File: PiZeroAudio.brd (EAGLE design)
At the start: 160 x 100 mm, 10 parts, among them J1 1X2-3.5MM

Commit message: Added I2C and Amplifier
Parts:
- added C10, C15, C16, C20, C22, C25: 1nF, resistor:C0805
- added C11, C26, C5, C6, C8, C9: 100nF, adafruit:C0805
- added C12: 100uF, adafruit:C0805
- added C13, C17, C18, C23: 220nF, resistor:C0805
- added C14, C19, C21, C24: 1uF, resistor:C0805
- added C27: 100UF, adafruit:C0805
- added C7: 47uF, adafruit:085CS_1AR
- added CN1: 1X4-BIG, adafruit:1X04-BIG
- added L1, L2, L3, L4: BLM31A, HappyBrackets:SML1206
- added R10: 39K, adafruit:R0805
- added R11: 56K, adafruit:R0805
- added R12, R13, R14: 33K, adafruit:R0805
- added R15: 10R, adafruit:R0805
- added R5, R8: 1K8, adafruit:R0805
- added R6: 220, adafruit:R0805
- added R7: 100, adafruit:R0805
- added R9: 10K, adafruit:R0805
- added U1: (no value), adafruit:TSSOP14
- added U2: (no value), HappyBrackets:LGA-16-3X3
- added U3: NC7WZ16, fairchild:SC-70-6
- added U4: TPA3144D2PWPR, HappyBrackets:HTSSOP28
- C1, C2: value 33nF -> 100nF
- C4: value 47uF -> 100nF; device adafruit:085CS_1AR -> adafruit:C0805
- R1: value 270 -> 10K
- R2: value 150 -> 10K
- R3: value 270 -> 220
- R4: value 150 -> 100
- moved R2 118.0 mm to (-82.5, -53.3)
- moved C2 98.0 mm to (-82.5, -59.7)
- moved R1 84.4 mm to (-82.5, -47.0)
- moved C1 82.4 mm to (-82.5, -40.6)
- moved R3 39.4 mm to (-59.7, 34.3)
- moved C4 10.5 mm to (-48.3, 34.3)
- moved R4 10.2 mm to (-16.5, 44.5)
- renumbered U$1 to CON1
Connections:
- new net +3V3: C1.1, C5.1, C6.1, C8.1, CON1.1, R1.1, R2.1, U1.1, U2.1, U2.16, U2.4, U2.5, U3.5
- new net /MUTE: R9.1
- new net AUDIO-L: C3.-, R5.2
- new net AUDIO-R: C7.-, R8.2, U4.12
- new net N$10: C23.2, U4.17
- new net N$11: C16.2, CN1.2, L2.C
- new net N$12: C15.1, CN1.1, L1.C
- new net N$13: C18.2, U4.21
- new net N$14: C20.1, CN1.3, L3.C
- new net N$15: C22.2, CN1.4, L4.C
- new net N$16: C17.2, U4.22
- new net N$17: C13.2, U4.26
- new net N$18: C13.1, L1.A, U4.25
- new net N$19: C17.1, L2.A, U4.23
- new net N$2: R3.2, U3.6
- new net N$20: C18.1, L3.A, U4.20
- new net N$21: C23.1, L4.A, U4.18
- new net N$23: R12.1, R13.2, U4.6
- new net N$24: R13.1, R14.2, U4.7
- new net N$25: R10.1, R11.2, U4.8
- new net N$26: C19.1, R11.1, R14.1, U4.5, U4.9
- new net N$4: C7.+, C9.1, R6.1, R7.2
- new net N$5: R9.2, U4.1, U4.2
- new net N$6: U4.3
- new net N$7: C14.1, U4.4
- new net N$8: C21.1, U4.11
- new net N$9: C24.1, R15.1, U4.14
- new net SCL: CON1.5, R2.2, U2.2
- new net SDA: CON1.3, R1.2, U2.3
- net +5V: now also C10.1, C11.1, C12.1, C2.1, C25.1, C26.1, C27.1, R15.2, U1.14, U4.15, U4.16, U4.27, U4.28
- net GND: now also C10.2, C11.2, C12.2, C14.2, C15.2, C16.1, C19.2, C20.2, C21.2, C22.1, C24.2, C25.2, C26.2, C27.2, C4.2, C5.2, C6.2, C8.2, C9.2, R10.2, R12.2, R5.1, R7.1, R8.1, U1.7, U2.10, U2.11, U2.12, U2.13, U2.15, U2.8, U2.9, U3.2, U4.10, U4.13, U4.19, U4.24; no longer R2.1
- net N$1: now also C4.1, R3.1, R4.2; no longer C1.1, R1.1, R2.2
- net N$3: now also R6.2, U3.4; no longer C2.1, C4.+, R3.1, R4.2
- net PWM-LEFT: now also U3.1; no longer R1.2
- net PWM-RIGHT: now also U3.3; no longer R3.2
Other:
- board size 160 x 100 mm -> 65.4 x 30.2 mm

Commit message: Renumbered Pins Placed components for first board
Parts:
- removed C27: 100UF, adafruit:C0805
- added JP1: GPIO, adafruit:2X04
- C10, C25: value 1nF -> 100nF; device resistor:C0805 -> adafruit:C0805
- C11: value 100nF -> 100uF; device adafruit:C0805 -> adafruit:CT3528
- C12: value 100uF -> 220nF; device adafruit:C0805 -> resistor:C0805
- C13, C18, C23: value 220nF -> 1uF
- C14, C19, C21, C24: value 1uF -> 1nF
- C16, C22: value 1nF -> 220nF
- C20: value 1nF -> 1uF
- C26: value 100nF -> 100UF; device adafruit:C0805 -> adafruit:CT3528
- C3: device adafruit:085CS_1AR -> adafruit:CT3528
- C6: value 100nF -> 47uF; device adafruit:C0805 -> adafruit:CT3528
- C7: value 47uF -> 100nF; device adafruit:085CS_1AR -> adafruit:C0805
- C9: value 100nF -> 1nF; device adafruit:C0805 -> resistor:C0805
- L1, L2, L3, L4: value BLM31A -> FB
- moved R14 287.2 mm to (-33.1, 3.30)
- moved R13 283.1 mm to (-33.1, 5.46), turned to 180 degrees
- moved R12 279.0 mm to (-33.1, 7.62)
- moved R11 269.9 mm to (-39.2, 6.10)
- moved R10 261.2 mm to (-39.1, 3.43), turned to 180 degrees
- moved C23 259.4 mm to (-46.0, 15.9)
- moved C19 253.7 mm to (-67.3, 7.49), turned to 90 degrees
- moved C18 249.0 mm to (-46.0, 11.6)
- moved C17 240.7 mm to (-58.5, 12.1)
- moved C13 234.1 mm to (-45.8, 8.89)
- moved C22 230.4 mm to (-58.5, 14.2)
- moved C20 226.4 mm to (-46.0, 13.7)
- moved C16 213.6 mm to (-58.5, 9.78)
- moved C15 203.8 mm to (-65.2, 7.49), turned to 270 degrees
- moved L4 202.4 mm to (-69.7, 13.2), turned to 90 degrees
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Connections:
- new net ACC-INT1: CON1.11, U2.6
- new net ACC-INT2: CON1.13, U2.7
- new net GPIO21: CON1.29, U1.2
- new net GPIO22: CON1.31, U1.3
- new net GPIO23: CON1.33, U1.4
- new net GPIO25: CON1.37, U1.5
- new net L+: C14.1, CN1.1, L1.C
- new net L-: C15.2, CN1.2, L2.C
- new net R+: C21.2, CN1.4, L4.C
- new net R-: C19.1, CN1.3, L3.C
- net +3V3: now also C7.1, CON1.17, U1.8; no longer C6.1, C8.1
- net +5V: now also C11.+, C24.1, C26.+, C9.1; no longer C11.1, C12.1, C26.1, C27.1
- net /MUTE: now also CON1.36
- net AUDIO-L: now also C6.-, R8.2; no longer C3.-, R5.2
- net AUDIO-R: now also C3.-, R5.2; no longer C7.-, R8.2
- net GND: now also C11.-, C13.2, C15.1, C18.2, C21.1, C23.2, C26.-, C7.2, JP1.2, JP1.4, JP1.6, JP1.8; no longer C11.2, C12.2, C15.2, C16.1, C21.2, C22.1, C26.2, C27.2, C6.2
- net N$10: now also C22.2; no longer C23.2
- net N$11: now also JP1.1, U1.13; no longer C16.2, CN1.2, L2.C
- net N$12: now also JP1.3, U1.12; no longer C15.1, CN1.1, L1.C
- net N$13: now also C17.2; no longer C18.2
- net N$14: now also JP1.5, U1.11; no longer C20.1, CN1.3, L3.C
- net N$15: now also JP1.7, U1.10; no longer C22.2, CN1.4, L4.C
- net N$16: now also C16.2; no longer C17.2
- net N$17: now also C12.2; no longer C13.2
- net N$18: now also C12.1; no longer C13.1
- net N$19: now also C16.1; no longer C17.1
- net N$20: now also C17.1; no longer C18.1
- net N$21: now also C22.1; no longer C23.1
- net N$26: now also C18.1; no longer C19.1
- net N$4: now also C6.+, C8.1; no longer C7.+, C9.1
- net N$7: now also C13.1; no longer C14.1
- net N$8: now also C20.1; no longer C21.1
- net N$9: now also C23.1; no longer C24.1
- net PWM-LEFT: now also U3.3; no longer U3.1
- net PWM-RIGHT: now also CON1.35, U3.1; no longer CON1.33, U3.3

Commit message: Updated
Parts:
- moved JP1 0.90 mm to (-16.6, 18.2)
- moved U2 0.42 mm to (-69.1, 20.1), turned to 270 degrees
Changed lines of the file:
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@@
 <element name="R5" library="adafruit" package="R0805" value="1K8" x="-33.655" y="10.922" rot="R270"/>
 <element name="R8" library="adafruit" package="R0805" value="1K8" x="-39.243" y="13.716"/>
-<element name="U2" library="HappyBrackets" library_urn="urn:adsk.eagle:library:5224691" package="LGA-16-3X3" package3d_urn="urn:adsk.eagle:package:5224694/1" value="" x="-68.7956" y="20.32" rot="R90"/>
+<element name="U2" library="HappyBrackets" library_urn="urn:adsk.eagle:library:5224691" package="LGA-16-3X3" package3d_urn="urn:adsk.eagle:package:5224694/1" value="" x="-69.1264" y="20.066" rot="R270"/>
 <element name="C5" library="adafruit" package="C0805" value="100nF" x="-68.8292" y="23.622"/>
 <element name="C1" library="adafruit" package="C0805" value="100nF" x="-49.53" y="23.241"/>
@@
 <element name="R13" library="adafruit" package="R0805" value="33K" x="-33.147" y="5.461" rot="R180"/>
 <element name="R14" library="adafruit" package="R0805" value="33K" x="-33.147" y="3.302"/>
-<element name="JP1" library="adafruit" package="2X04" value="GPIO" x="-16.51" y="19.05" rot="R270"/>
+<element name="JP1" library="adafruit" package="2X04" value="GPIO" x="-16.637" y="18.161" rot="R270"/>
 </elements>
 <signals>
@@
 <wire x1="-60.21" y1="26.5" x2="-55.13" y2="29.04" width="0" layer="19" extent="1-1"/>
 <wire x1="-65.29" y1="29.04" x2="-60.21" y2="26.5" width="0" layer="19" extent="1-1"/>
-<wire x1="-69.7956" y1="21.72" x2="-65.29" y2="29.04" width="0" layer="19" extent="1-1"/>
-<wire x1="-69.2956" y1="21.72" x2="-69.7956" y2="21.72" width="0" layer="19" extent="1-1"/>
-<wire x1="-68.7956" y1="21.72" x2="-69.2956" y2="21.72" width="0" layer="19" extent="1-1"/>
-<wire x1="-68.2956" y1="21.72" x2="-68.7956" y2="21.72" width="0" layer="19" extent="1-1"/>
-<wire x1="-67.7956" y1="21.72" x2="-68.2956" y2="21.72" width="0" layer="19" extent="1-1"/>
-<wire x1="-69.2956" y1="21.72" x2="-67.7956" y2="21.72" width="0" layer="19" extent="1-1"/>
-<wire x1="-70.1956" y1="20.32" x2="-69.7956" y2="21.72" width="0" layer="19" extent="1-1"/>
-<wire x1="-67.9792" y1="23.622" x2="-69.2956" y2="21.72" width="0" layer="19" extent="1-1"/>
-<wire x1="-73.152" y1="21.756" x2="-70.1956" y2="20.32" width="0" layer="19" extent="1-1"/>
+<wire x1="-68.1264" y1="18.666" x2="-65.29" y2="29.04" width="0" layer="19" extent="1-1"/>
+<wire x1="-68.6264" y1="18.666" x2="-68.1264" y2="18.666" width="0" layer="19" extent="1-1"/>
+<wire x1="-69.1264" y1="18.666" x2="-68.6264" y2="18.666" width="0" layer="19" extent="1-1"/>
+<wire x1="-69.6264" y1="18.666" x2="-69.1264" y2="18.666" width="0" layer="19" extent="1-1"/>
+<wire x1="-70.1264" y1="18.666" x2="-69.6264" y2="18.666" width="0" layer="19" extent="1-1"/>
+<wire x1="-68.6264" y1="18.666" x2="-70.1264" y2="18.666" width="0" layer="19" extent="1-1"/>
+<wire x1="-67.7264" y1="20.066" x2="-68.1264" y2="18.666" width="0" layer="19" extent="1-1"/>
+<wire x1="-67.9792" y1="23.622" x2="-68.6264" y2="18.666" width="0" layer="19" extent="1-1"/>
+<wire x1="-73.152" y1="21.756" x2="-67.7264" y2="20.066" width="0" layer="19" extent="1-1"/>
 <wire x1="-22.11" y1="26.5" x2="-29.73" y2="29.04" width="0" layer="19" extent="1-1"/>
-<wire x1="-15.24" y1="22.86" x2="-22.11" y2="26.5" width="0" layer="19" extent="1-1"/>
-<wire x1="-15.24" y1="20.32" x2="-15.24" y2="22.86" width="0" layer="19" extent="1-1"/>
-<wire x1="-15.24" y1="17.78" x2="-15.24" y2="20.32" width="0" layer="19" extent="1-1"/>
-<wire x1="-15.24" y1="15.24" x2="-15.24" y2="17.78" width="0" layer="19" extent="1-1"/>
+<wire x1="-15.367" y1="21.971" x2="-22.11" y2="26.5" width="0" layer="19" extent="1-1"/>
+<wire x1="-15.367" y1="19.431" x2="-15.367" y2="21.971" width="0" layer="19" extent="1-1"/>
+<wire x1="-15.367" y1="16.891" x2="-15.367" y2="19.431" width="0" layer="19" extent="1-1"/>
+<wire x1="-15.367" y1="14.351" x2="-15.367" y2="16.891" width="0" layer="19" extent="1-1"/>
 </signal>
 <signal name="PWM-LEFT">
@@
 <contactref element="CON1" pad="17"/>
 <contactref element="U1" pad="8"/>
-<wire x1="-67.7956" y1="18.92" x2="-69.6792" y2="23.622" width="0" layer="19" extent="1-1"/>
-<wire x1="-68.2956" y1="18.92" x2="-67.7956" y2="18.92" width="0" layer="19" extent="1-1"/>
-<wire x1="-69.7956" y1="18.92" x2="-68.2956" y2="18.92" width="0" layer="19" extent="1-1"/>
-<wire x1="-68.2956" y1="18.92" x2="-69.7956" y2="18.92" width="0" layer="19" extent="1-1"/>
-<wire x1="-70.37" y1="26.5" x2="-68.2956" y2="18.92" width="0" layer="19" extent="1-1"/>
-<wire x1="-64.516" y1="21.733" x2="-68.2956" y2="18.92" width="0" layer="19" extent="1-1"/>
+<wire x1="-70.1264" y1="21.466" x2="-69.6792" y2="23.622" width="0" layer="19" extent="1-1"/>
+<wire x1="-69.6264" y1="21.466" x2="-70.1264" y2="21.466" width="0" layer="19" extent="1-1"/>
+<wire x1="-68.1264" y1="21.466" x2="-69.6264" y2="21.466" width="0" layer="19" extent="1-1"/>
+<wire x1="-69.6264" y1="21.466" x2="-68.1264" y2="21.466" width="0" layer="19" extent="1-1"/>
+<wire x1="-70.37" y1="26.5" x2="-69.6264" y2="21.466" width="0" layer="19" extent="1-1"/>
+<wire x1="-64.516" y1="21.733" x2="-69.6264" y2="21.466" width="0" layer="19" extent="1-1"/>
 <wire x1="-61.722" y1="21.733" x2="-64.516" y2="21.733" width="0" layer="19" extent="1-1"/>
 <wire x1="-50.38" y1="23.241" x2="-61.722" y2="21.733" width="0" layer="19" extent="1-1"/>
@@
 <contactref element="R1" pad="2"/>
 <contactref element="U2" pad="3"/>
-<wire x1="-68.7956" y1="18.92" x2="-64.516" y2="23.733" width="0" layer="19" extent="1-1"/>
-<wire x1="-67.83" y1="26.5" x2="-68.7956" y2="18.92" width="0" layer="19" extent="1-1"/>
+<wire x1="-69.1264" y1="21.466" x2="-64.516" y2="23.733" width="0" layer="19" extent="1-1"/>
+<wire x1="-67.83" y1="26.5" x2="-69.1264" y2="21.466" width="0" layer="19" extent="1-1"/>
 </signal>
 <signal name="SCL">
@@
 <contactref element="R2" pad="2"/>
 <contactref element="U2" pad="2"/>
-<wire x1="-69.2956" y1="18.92" x2="-61.722" y2="23.733" width="0" layer="19" extent="1-1"/>
-<wire x1="-65.29" y1="26.5" x2="-69.2956" y2="18.92" width="0" layer="19" extent="1-1"/>
+<wire x1="-68.6264" y1="21.466" x2="-61.722" y2="23.733" width="0" layer="19" extent="1-1"/>
+<wire x1="-65.29" y1="26.5" x2="-68.6264" y2="21.466" width="0" layer="19" extent="1-1"/>
 </signal>
 <signal name="N$5">
@@
 <contactref element="U2" pad="6"/>
 <contactref element="CON1" pad="11"/>
-<wire x1="-57.67" y1="26.5" x2="-67.3956" y2="19.82" width="0" layer="19" extent="1-1"/>
+<wire x1="-57.67" y1="26.5" x2="-70.5264" y2="20.566" width="0" layer="19" extent="1-1"/>
 </signal>
 <signal name="ACC-INT2">
 <contactref element="CON1" pad="13"/>
 <contactref element="U2" pad="7"/>
-<wire x1="-55.13" y1="26.5" x2="-67.3956" y2="20.32" width="0" layer="19" extent="1-1"/>
+<wire x1="-55.13" y1="26.5" x2="-70.5264" y2="20.066" width="0" layer="19" extent="1-1"/>
 </signal>
 <signal name="N$11">
 <contactref element="U1" pad="13"/>
 <contactref element="JP1" pad="1"/>
-<wire x1="-21.9742" y1="23.271" x2="-17.78" y2="22.86" width="0" layer="19" extent="1-1"/>
+<wire x1="-21.9742" y1="23.271" x2="-17.907" y2="21.971" width="0" layer="19" extent="1-1"/>
 </signal>
 <signal name="N$12">
 <contactref element="U1" pad="12"/>
 <contactref element="JP1" pad="3"/>
-<wire x1="-21.9742" y1="22.621" x2="-17.78" y2="20.32" width="0" layer="19" extent="1-1"/>
+<wire x1="-21.9742" y1="22.621" x2="-17.907" y2="19.431" width="0" layer="19" extent="1-1"/>
 </signal>
 <signal name="N$14">
 <contactref element="U1" pad="11"/>
 <contactref element="JP1" pad="5"/>
-<wire x1="-21.9742" y1="21.971" x2="-17.78" y2="17.78" width="0" layer="19" extent="1-1"/>
+<wire x1="-21.9742" y1="21.971" x2="-17.907" y2="16.891" width="0" layer="19" extent="1-1"/>
 </signal>
 <signal name="N$15">
 <contactref element="U1" pad="10"/>
 <contactref element="JP1" pad="7"/>
-<wire x1="-21.9742" y1="21.321" x2="-17.78" y2="15.24" width="0" layer="19" extent="1-1"/>
+<wire x1="-21.9742" y1="21.321" x2="-17.907" y2="14.351" width="0" layer="19" extent="1-1"/>
 </signal>
 <signal name="GPIO23">

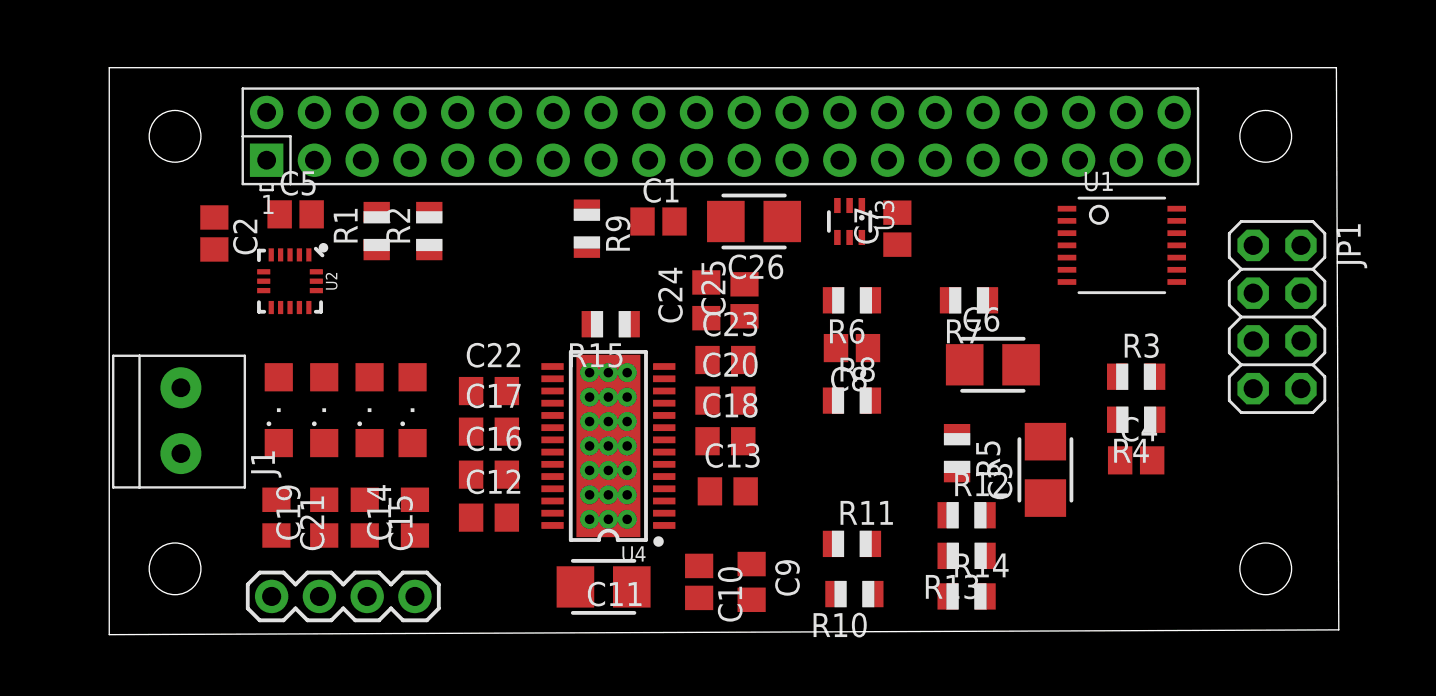
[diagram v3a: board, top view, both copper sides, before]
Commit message: Pre-resync board and schematic There is board inconsitency
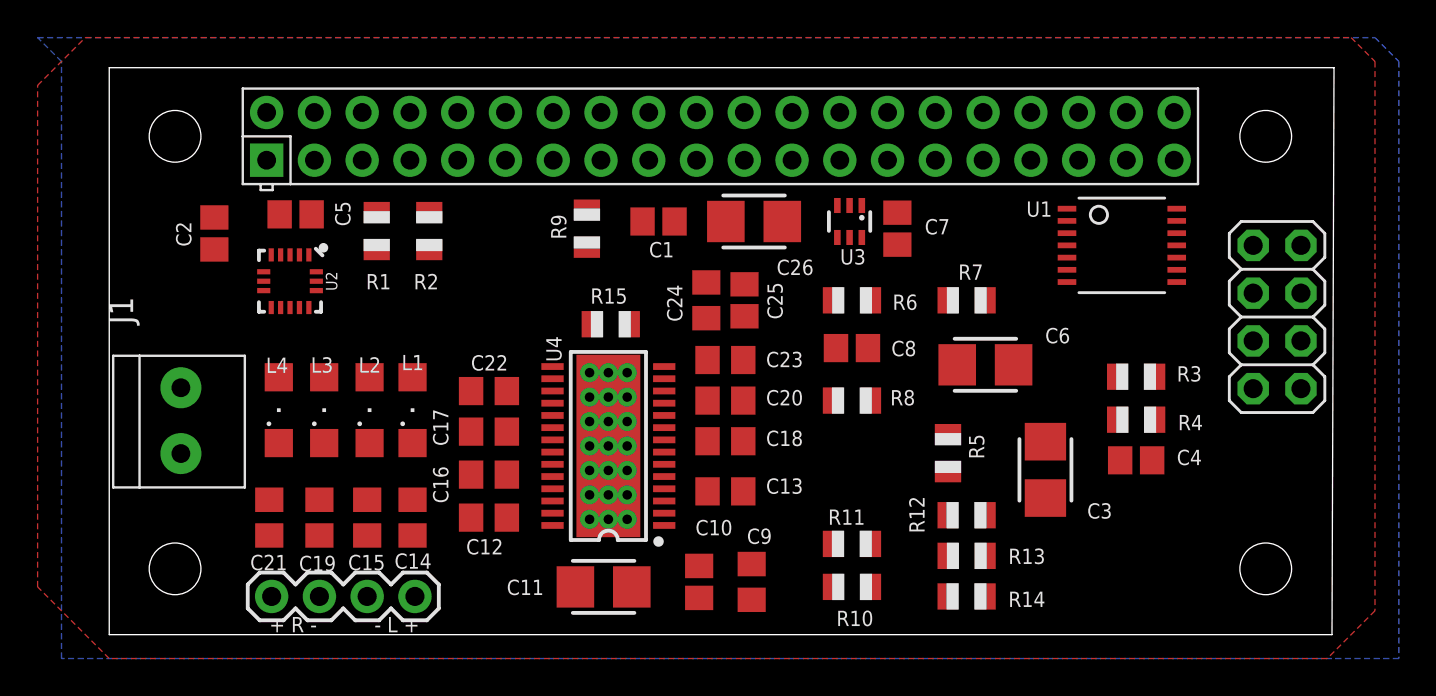
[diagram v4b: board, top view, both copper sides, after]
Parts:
- moved R5 0.48 mm to (-34.1, 10.9)
- moved R10 0.40 mm to (-39.2, 3.81)
- moved C6 0.40 mm to (-32.1, 15.6)
- moved C21 0.38 mm to (-70.2, 7.49)
- moved C19 0.25 mm to (-67.6, 7.49)
- moved C13 0.13 mm to (-46.0, 8.89)
- moved C14 0.13 mm to (-62.6, 7.49)
- moved C15 0.13 mm to (-65.0, 7.49)
- moved R7 0.13 mm to (-33.1, 19.1)
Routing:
- added copper zone on layer 1, net GND
- added copper zone on layer 16, net GND
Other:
- board size 65.4 x 30.2 mm -> 65.1 x 30.2 mm
- board text added: "+ R -"
- board text added: "- L +"
